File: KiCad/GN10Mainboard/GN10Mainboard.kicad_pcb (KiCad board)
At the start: 4 copper layers, 80 x 60 mm, 130 parts, among them J1 XT30PW-M, J10 USB_C_Receptacle_USB2.0, J12 Conn_01x04, J13 Conn_01x06, J14 Conn_01x06, J4 Conn_01x04, J5 Conn_01x06, J6 Conn_01x04, J7 Conn_01x04, J8 Conn_01x04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

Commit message: update:GND zorn
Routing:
- net GND: vias 37 -> 40
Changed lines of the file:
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@@
+	)
+	(via
+		(at 142.1 117.4)
+		(size 0.6)
+		(drill 0.3)
+		(layers "F.Cu" "B.Cu")
+		(free yes)
+		(net 1)
 	)
 	(via
@@
 	)
 	(via
+		(at 142.1 118.2)
+		(size 0.6)
+		(drill 0.3)
+		(layers "F.Cu" "B.Cu")
+		(free yes)
+		(net 1)
+	)
+	(via
 		(at 142.1 122.7)
 		(size 0.6)
@@
 	(via
 		(at 134.6 122.6)
+		(size 0.6)
+		(drill 0.3)
+		(layers "F.Cu" "B.Cu")
+		(free yes)
+		(net 1)
+	)
+	(via
+		(at 142.1 119)
 		(size 0.6)
 		(drill 0.3)
@@
 	)
 	(zone
+		(net 0)
+		(net_name "")
+		(layer "F.Cu")
+		(hatch edge 0.5)
+		(connect_pads
+			(clearance 0)
+		)
+		(min_thickness 0.25)
+		(filled_areas_thickness no)
+		(keepout
+			(tracks allowed)
+			(vias allowed)
+			(pads allowed)
+			(copperpour not_allowed)
+			(footprints allowed)
+		)
+		(placement
+			(enabled no)
+			(sheetname "")
+		)
+		(fill
+			(thermal_gap 0.5)
+			(thermal_bridge_width 0.5)
+		)
+		(polygon
+			(pts
+				(xy 134.8 128.2) (xy 134.8 132.8) (xy 136.2 132.8) (xy 136.2 128.2)
+			)
+		)
+	)
+	(zone
 		(net 9)
 		(net_name "Net-(D2-K)")
@@
 			)
 		)
+	)
+	(zone
+		(net 0)
+		(net_name "")
+		(layer "F.Cu")
+		(hatch edge 0.5)
+		(connect_pads
+			(clearance 0)
+		)
+		(min_thickness 0.25)
+		(filled_areas_thickness no)
+		(keepout
+			(tracks allowed)
+			(vias allowed)
+			(pads allowed)
+			(copperpour not_allowed)
+			(footprints allowed)
+		)
+		(placement
+			(enabled no)
+			(sheetname "")
+		)
+		(fill
+			(thermal_gap 0.5)
+			(thermal_bridge_width 0.5)
+		)
+		(polygon
+			(pts
+				(xy 135.9 122.2) (xy 135.9 125.3) (xy 137.3 125.3) (xy 137.3 122.2)
+			)
+		)

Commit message: update:wiring
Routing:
- net +3.3V: track 237.3 -> 376.1 mm, vias 0 -> 9
- net GNDS: track 0.00 -> 22.7 mm
- net VBUS: track 0.00 -> 20.3 mm
- net GYRO_INT: track 0.00 -> 16.8 mm, vias 0 -> 2
- net GYRO_RESET: track 2.14 -> 16.3 mm, vias 0 -> 2
- net Net-(U11-CBUS2): track 0.00 -> 12.9 mm, vias 0 -> 2
- net USBD+: track 0.00 -> 11.0 mm, vias 0 -> 2
- net I2C3_SDA: track 0.00 -> 10.7 mm, vias 0 -> 2
- net USBD-: track 0.00 -> 9.98 mm, vias 0 -> 2
- net I2C3_SCL: track 0.00 -> 8.27 mm, vias 0 -> 2
- net Net-(J9-TCT): track 0.00 -> 4.14 mm
- net Net-(J10-CC2): track 0.00 -> 2.82 mm
- net Net-(U4-PB8): track 0.00 -> 2.34 mm
- net Net-(J10-CC1): track 0.00 -> 2.14 mm
- net Net-(U10-XOUT32): track 3.75 -> 5.47 mm
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
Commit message: update
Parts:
- removed J12: Conn_01x04, Connector_JST:JST_XH_B4B-XH-A_1x04_P2.50mm_Vertical
- moved R26 3.63 mm to (187.1, 101.6), turned to 0 degrees
- moved R25 3.13 mm to (187.1, 103.0), turned to 0 degrees
- moved R9 0.10 mm to (188.1, 120.3)
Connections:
- U11 pad 20: USART2_RX -> USART1_RX
- U11 pad 4: USART2_TX -> USART1_TX
- U4 pad 14: USART2_TX -> unconnected-(U4-PA2-Pad14)
- U4 pad 17: USART2_RX -> unconnected-(U4-PA3-Pad17)
- U4 pad 34: LED_RED -> unconnected-(U4-PB12-Pad34)
- U4 pad 35: LED_GREEN -> unconnected-(U4-PB13-Pad35)
- U4 pad 36: LED_BLUE -> unconnected-(U4-PB14-Pad36)
- U4 pad 43: unconnected-(U4-PA9-Pad43) -> USART1_TX
- U4 pad 44: unconnected-(U4-PA10-Pad44) -> USART1_RX
- U4 pad 52: SW1 -> LED_RED
- U4 pad 53: SW2 -> LED_GREEN
- U4 pad 54: SW3 -> LED_BLUE
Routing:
- net STM32_RESET: track 1.44 -> 42.4 mm, vias 0 -> 2
- net TIM1_CH1: track 0.00 -> 37.5 mm, vias 0 -> 1
- net CAN1_TX: track 0.00 -> 35.6 mm, vias 0 -> 2
- net SYS_SWDIO: track 0.00 -> 34.0 mm, vias 0 -> 1
- net SYS_SWCLK: track 0.00 -> 32.9 mm, vias 0 -> 1
- net CAN1_RX: track 0.00 -> 32.1 mm, vias 0 -> 2
- net TIM1_CH2: track 0.00 -> 26.8 mm, vias 0 -> 2
- net USART1_RX: track 0.00 -> 22.6 mm, vias 0 -> 2
- net TIM2_CH1: track 0.00 -> 18.0 mm
- net TIM2_CH2: track 0.00 -> 17.7 mm
- net USART1_TX: track 0.00 -> 16.7 mm, vias 0 -> 2
- net LED_BLUE: track 0.00 -> 13.9 mm
- net LED_GREEN: track 0.00 -> 12.5 mm
- net LED_RED: track 0.00 -> 12.2 mm
- net +3.3V: track 376.1 -> 374.1 mm, vias 9 -> 10
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
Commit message: fix:feedback wire
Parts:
- moved R12 5.39 mm to (134.7, 133.4), turned to 90 degrees
- moved R13 5.15 mm to (134.2, 131.5), turned to 180 degrees
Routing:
- net Net-(U1-FB): track 9.69 -> 3.57 mm
- net +5V: track 98.4 -> 103.9 mm
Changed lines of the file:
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@@
 	(footprint "Resistor_SMD:R_0402_1005Metric"
 		(layer "F.Cu")
-		(at 136.7 136)
+		(at 134.2 131.5 180)
 		(descr "Resistor SMD 0402 (1005 Metric), square (rectangular) end terminal, IPC-7351 nominal, (Body size source: IPC-SM-782 page 72, https://www.pcb-3d.com/wordpress/wp-content/uploads/ipc-sm-782a_amendment_1_and_2.pdf), generated with kicad-footprint-generator")
 		(tags "resistor")
@@
 		(attr smd)
 		(fp_line
-			(start -0.153641 -0.38)
-			(end 0.153641 -0.38)
+			(start -0.153641 0.38)
+			(end 0.153641 0.38)
 			(stroke
 				(width 0.12)
@@
 		)
 		(fp_line
-			(start -0.153641 0.38)
-			(end 0.153641 0.38)
+			(start -0.153641 -0.38)
+			(end 0.153641 -0.38)
 			(stroke
 				(width 0.12)
@@
 		)
 		(fp_line
-			(start -0.93 -0.47)
-			(end 0.93 -0.47)
+			(start 0.93 0.47)
+			(end -0.93 0.47)
 			(stroke
 				(width 0.05)
@@
 		)
 		(fp_line
-			(start -0.93 0.47)
-			(end -0.93 -0.47)
+			(start 0.93 -0.47)
+			(end 0.93 0.47)
 			(stroke
 				(width 0.05)
@@
 		)
 		(fp_line
-			(start 0.93 -0.47)
-			(end 0.93 0.47)
+			(start -0.93 0.47)
+			(end -0.93 -0.47)
 			(stroke
 				(width 0.05)
@@
 		)
 		(fp_line
-			(start 0.93 0.47)
-			(end -0.93 0.47)
+			(start -0.93 -0.47)
+			(end 0.93 -0.47)
 			(stroke
 				(width 0.05)
@@
 		)
 		(fp_line
-			(start -0.525 -0.27)
-			(end 0.525 -0.27)
+			(start 0.525 0.27)
+			(end -0.525 0.27)
 			(stroke
 				(width 0.1)
@@
 		)
 		(fp_line
-			(start -0.525 0.27)
-			(end -0.525 -0.27)
+			(start 0.525 -0.27)
+			(end 0.525 0.27)
 			(stroke
 				(width 0.1)
@@
 		)
 		(fp_line
-			(start 0.525 -0.27)
-			(end 0.525 0.27)
+			(start -0.525 0.27)
+			(end -0.525 -0.27)
 			(stroke
 				(width 0.1)
@@
 		)
 		(fp_line
-			(start 0.525 0.27)
-			(end -0.525 0.27)
+			(start -0.525 -0.27)
+			(end 0.525 -0.27)
 			(stroke
 				(width 0.1)
@@
 		)
 		(pad "1" smd roundrect
-			(at -0.51 0)
+			(at -0.51 0 180)
 			(size 0.54 0.64)
 			(layers "F.Cu" "F.Mask" "F.Paste")
@@
 		)
 		(pad "2" smd roundrect
-			(at 0.51 0)
+			(at 0.51 0 180)
 			(size 0.54 0.64)
 			(layers "F.Cu" "F.Mask" "F.Paste")
@@
 	(footprint "Resistor_SMD:R_0402_1005Metric"
 		(layer "F.Cu")
-		(at 136.7175 138.4 180)
+		(at 134.7 133.4 90)
 		(descr "Resistor SMD 0402 (1005 Metric), square (rectangular) end terminal, IPC-7351 nominal, (Body size source: IPC-SM-782 page 72, https://www.pcb-3d.com/wordpress/wp-content/uploads/ipc-sm-782a_amendment_1_and_2.pdf), generated with kicad-footprint-generator")
 		(tags "resistor")
 		(property "Reference" "R12"
-			(at 0 -1.17 0)
+			(at 0 -1.17 90)
 			(layer "F.SilkS")
 			(effects
@@
 		)
 		(property "Value" "53.6k"
-			(at 0 1.17 0)
+			(at 0 1.17 90)
 			(layer "F.Fab")
 			(effects
@@
 		)
 		(property "Datasheet" "~"
-			(at 0 0 0)
+			(at 0 0 90)
 			(layer "F.Fab")
 			(hide yes)
@@
 		)
 		(property "Description" "Resistor"
-			(at 0 0 0)
+			(at 0 0 90)
 			(layer "F.Fab")
 			(hide yes)
@@
 		(attr smd)
 		(fp_line
-			(start -0.153641 0.38)
-			(end 0.153641 0.38)
+			(start -0.153641 -0.38)
+			(end 0.153641 -0.38)
 			(stroke
 				(width 0.12)
@@
 		)
 		(fp_line
-			(start -0.153641 -0.38)
-			(end 0.153641 -0.38)
+			(start -0.153641 0.38)
+			(end 0.153641 0.38)
 			(stroke
 				(width 0.12)
@@
 		)
 		(fp_line
-			(start 0.93 0.47)
-			(end -0.93 0.47)
+			(start 0.93 -0.47)
+			(end 0.93 0.47)
 			(stroke
 				(width 0.05)
@@
 		)
 		(fp_line
-			(start 0.93 -0.47)
-			(end 0.93 0.47)
+			(start -0.93 -0.47)
+			(end 0.93 -0.47)
 			(stroke
 				(width 0.05)
@@
 		)
 		(fp_line
-			(start -0.93 0.47)
-			(end -0.93 -0.47)
+			(start 0.93 0.47)
+			(end -0.93 0.47)
 			(stroke
 				(width 0.05)
@@
 		)
 		(fp_line
-			(start -0.93 -0.47)
-			(end 0.93 -0.47)
+			(start -0.93 0.47)
+			(end -0.93 -0.47)
 			(stroke
 				(width 0.05)
@@
 		)
 		(fp_line
-			(start 0.525 0.27)
-			(end -0.525 0.27)
+			(start 0.525 -0.27)
+			(end 0.525 0.27)
 			(stroke
 				(width 0.1)
@@
 		)
 		(fp_line
-			(start 0.525 -0.27)
-			(end 0.525 0.27)
+			(start -0.525 -0.27)
+			(end 0.525 -0.27)
 			(stroke
 				(width 0.1)
@@
 		)
 		(fp_line
-			(start -0.525 0.27)
-			(end -0.525 -0.27)
+			(start 0.525 0.27)
+			(end -0.525 0.27)
 			(stroke
 				(width 0.1)
@@
 		)
 		(fp_line
-			(start -0.525 -0.27)
-			(end 0.525 -0.27)
+			(start -0.525 0.27)
+			(end -0.525 -0.27)
 			(stroke
 				(width 0.1)
@@
 		)
 		(fp_text user "${REFERENCE}"
-			(at 0 0 0)
+			(at 0 0 90)
 			(layer "F.Fab")
 			(effects
@@
 		)
 		(pad "1" smd roundrect
-			(at -0.51 0 180)
+			(at -0.51 0 90)
 			(size 0.54 0.64)
 			(layers "F.Cu" "F.Mask" "F.Paste")
@@
 		)
 		(pad "2" smd roundrect
-			(at 0.51 0 180)
+			(at 0.51 0 90)
 			(size 0.54 0.64)
 			(layers "F.Cu" "F.Mask" "F.Paste")
@@
 	)
 	(segment
+		(start 134.7 135.8725)
+		(end 137.2275 138.4)
+		(width 0.25)
+		(layer "F.Cu")
+		(net 4)
+	)
+	(segment
 		(start 144.352651 97.647349)
 		(end 146 96)
@@
 	)
 	(segment
+		(start 134.7 133.91)
+		(end 134.7 135.8725)
+		(width 0.25)
+		(layer "F.Cu")
+		(net 4)
+	)
+	(segment
 		(start 151.554999 111.52)
 		(end 155.1 111.52)
@@
 	(segment
 		(start 134.7175 129.325)
-		(end 134.7175 133.93576)
-		(width 0.3)
-		(layer "F.Cu")
-		(net 77)
-	)
-	(segment
-		(start 136.19 136)
-		(end 136.19 138.3825)
-		(width 0.3)
-		(layer "F.Cu")
-		(net 77)
-	)
-	(segment
-		(start 136.19 135.40826)
-		(end 136.19 136)
-		(width 0.3)
-		(layer "F.Cu")
-		(net 77)
-	)
-	(segment
-		(start 134.7175 133.93576)
-		(end 136.19 135.40826)
-		(width 0.3)
+		(end 134.7175 132.8725)
+		(width 0.25)
 		(layer "F.Cu")
 		(net 77)
 	)
 	(segment
-		(start 136.19 138.3825)
-		(end 136.2075 138.4)
-		(width 0.3)
+		(start 134.7175 132.8725)
+		(end 134.7 132.89)
+		(width 0.25)
 		(layer "F.Cu")
 		(net 77)

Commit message: update:wired all components
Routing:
- net Net-(J9-PadL2): track 0.00 -> 33.1 mm
- net Net-(J9-PadL4): track 0.00 -> 22.9 mm
- net ACT: track 0.00 -> 17.1 mm, vias 0 -> 2
- net LNK: track 0.00 -> 15.2 mm, vias 0 -> 2
- net Net-(U4-PC15): track 4.53 -> 6.27 mm
- net Net-(U4-PC14): track 5.36 -> 7.10 mm
- net SYS_SWCLK: track 32.9 -> 33.7 mm
- net GND: vias 40 -> 244

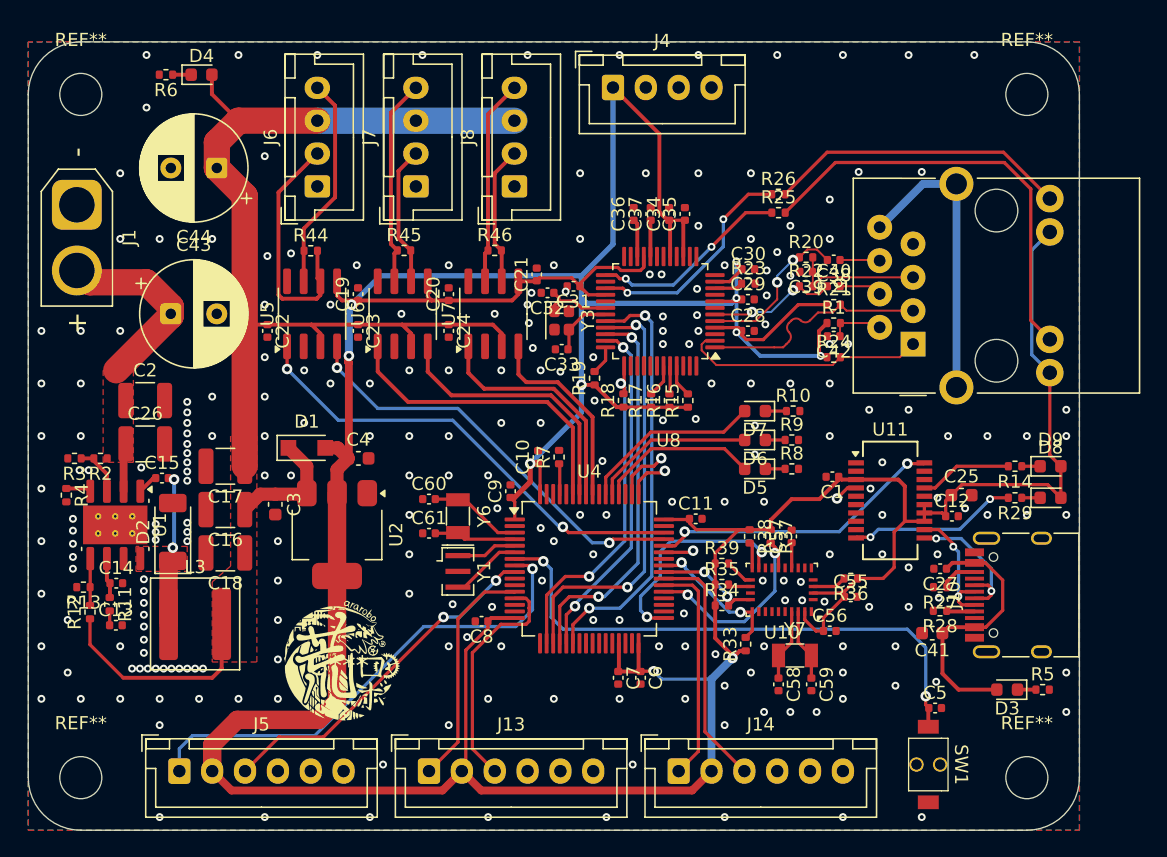
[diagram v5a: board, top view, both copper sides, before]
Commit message: update:silkscreen placement
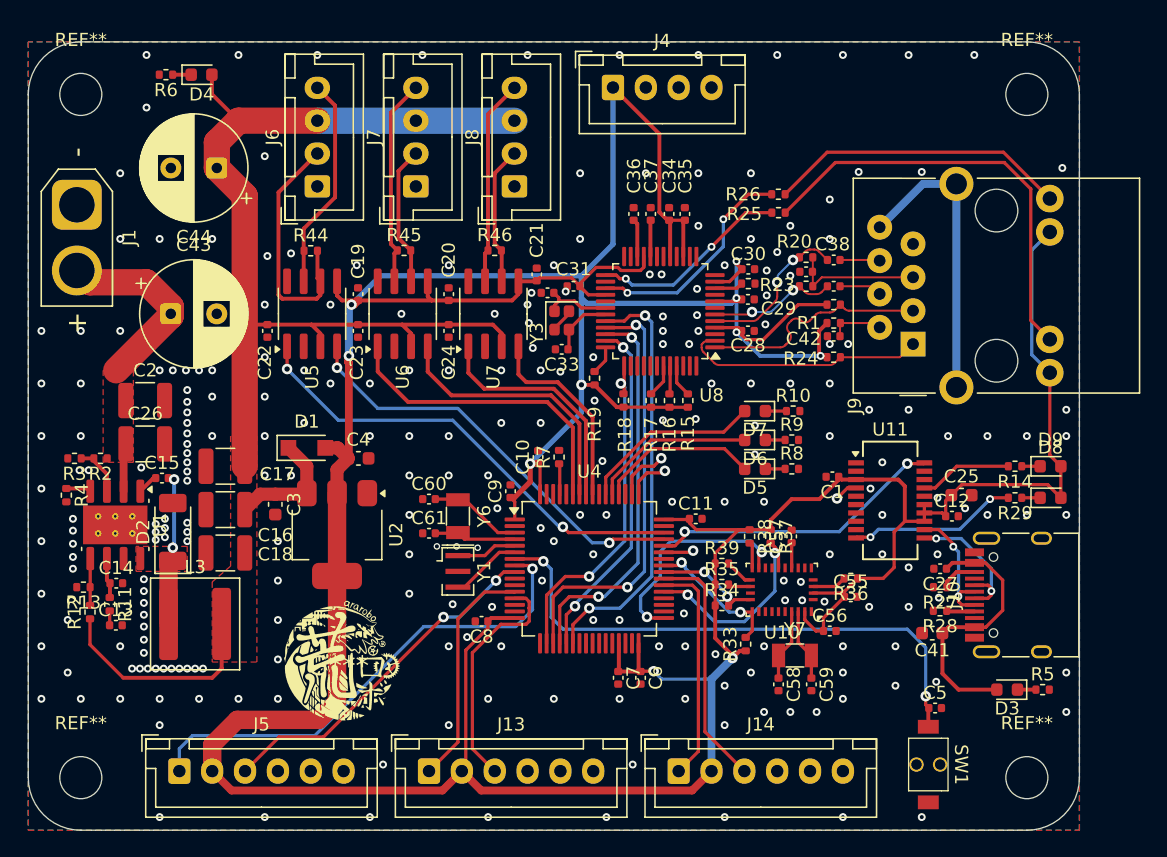
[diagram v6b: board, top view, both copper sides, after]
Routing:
- net GND: track 0.00 -> 1.86 mm, vias 244 -> 256

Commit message: add:gaber
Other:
- board text added: "CAN1"
- board text added: "CAN2"
- board text added: "CAN3"
- board text added: "GN10Mainboard v3.0"
- board text added: "Power"
- board text added: "STLink"
- board text added: "TIM1"
- board text added: "TIM2"
- board text added: "TIM3"
- board text added: "designed by aiba-gento"
